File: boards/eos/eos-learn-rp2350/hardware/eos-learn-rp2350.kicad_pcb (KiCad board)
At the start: 4 copper layers, 52.6 x 51.6 mm, 53 parts, among them J1 USB-C, J2 GPIO 0-15, J3 Power, GPIO 16-29, J4 SWD, J5 Qwiic, SW1 BOOTSEL, SW2 RUN, U1 RP2350A, U2 USBLC6-2SC6, U3 AP7361C-33, U4 W25Q128JVS, Y1 12MHz

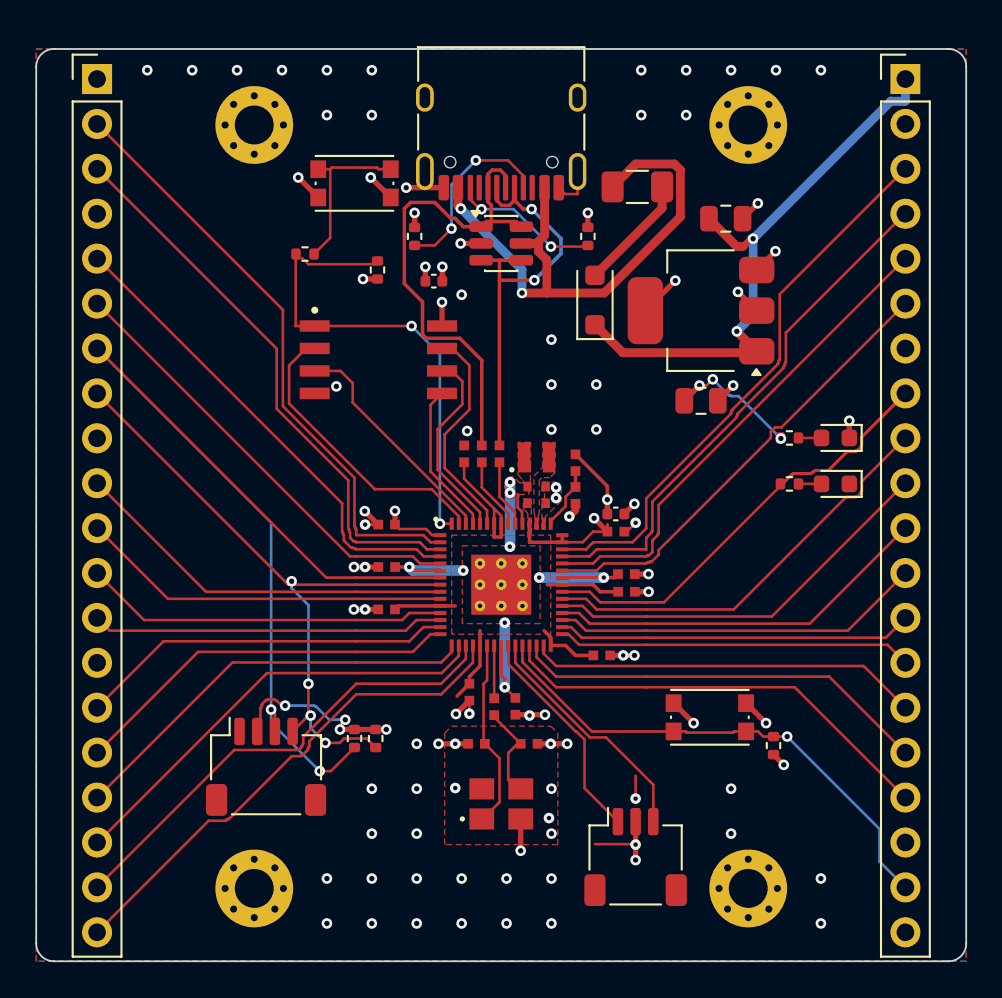
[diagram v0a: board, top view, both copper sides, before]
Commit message: fix(boards): USB-C receptacles at HRO's recommended edge distance
Each HRO TYPE-C-31-M-12 now sits with its footprint origin 3.19 mm from the
board edge it faces (design.USB_C_EDGE). HRO's "RECOMMEND P.C.B LAYOUT" draws
the PCB edge 5.79 mm from the locating pegs, which are 2.60 mm behind the
origin. At the old 3.8 mm the shell's face was 0.15 mm behind the edge, so a
plug's overmold could meet the board before the plug seated; the shell now
stands about 0.46 mm proud of it.

EoS Learn RP2350, EoS Probe S3 and EoS CM5 Base are moved and rebuilt: all
three report ERC 0, DRC errors 0, unconnected 0, schematic parity 0, with the
same DRC warnings as before (4, 4 and 6). On EoS CM5 Base, GPIO2 (the
header's SDA, CM5 pin 58) is now a priority route: after the move the
autorouter boxed its pad in twice, also with 100 passes.

UsbCEdgeTest checks every board's receptacles against the constant, within
the drawing's 0.05 mm tolerance. It fails for the old 3.8 mm placement.

Found in the independent review of a later board (EoS TM4C123 Board, M1).
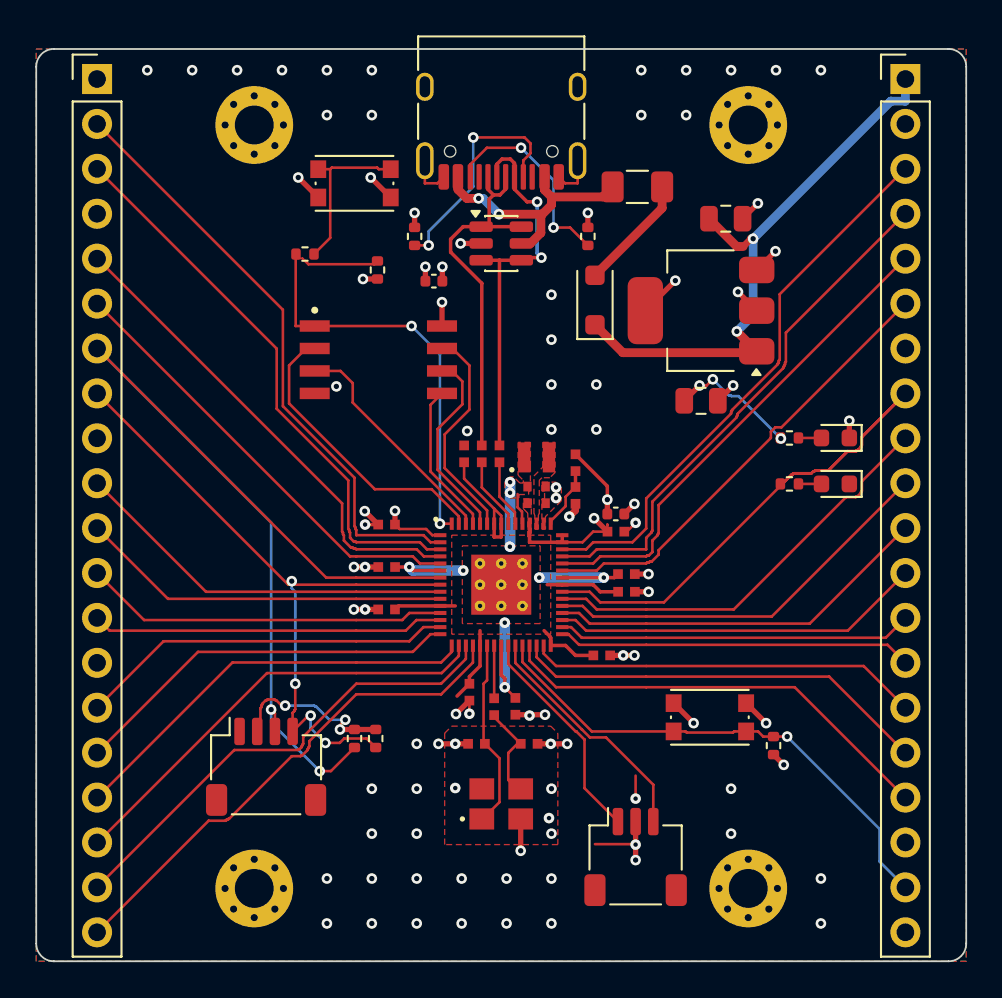
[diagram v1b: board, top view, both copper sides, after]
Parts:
- moved J1 0.61 mm to (26.3, 3.19)
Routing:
- net VBUS: track 32.6 -> 14.7 mm
- net /USB_D+: track 28.6 -> 21.3 mm
- net /CC2: track 8.45 -> 11.6 mm
- net /CC1: track 10.6 -> 13.4 mm
- net /USB_D-: track 23.9 -> 22.2 mm
- net /GPIO5: track 38.6 -> 39.3 mm
- net +3V3: track 61.0 -> 60.4 mm, vias 15 -> 14
- net GND: track 50.9 -> 51.3 mm, vias 89 -> 88

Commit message: fix(boards): rebuild the ten boards made before the no-via-in-pad rule (#55)
PR #64's generator keeps vias out of surface pads (a chip's exposed pad
aside) and 0.1 mm from their own net's pads. Ten boards on master were built
before that rule and had 34 pads with a via in or beside them. They are
rebuilt with the same generator: ATmega328P, RA2E1, KE16Z, KL25, STM32 64,
ESP32 DevKit, Learn RP2350, LPC55S69, CM4 Base and CM5 Base. Each builds at
ERC 0, DRC errors 0, unconnected 0 and parity 0, with the same parts, values,
nets and positions and the same DRC warnings as before.

Where the router could no longer close a short link without a via in a pad,
or left a ground pad without a good path to a via, the design files use
routing options only: priority routes, fanout_first, ground_vias, and a
bottom-layer router keep-out under KL25's crystal (so RESET_b no longer runs
under it). ViaInPadTest drops BUILT_BEFORE_THE_RULE; it now allows only Learn
RP2350's two Raspberry Pi reference vias, named by position. READMEs, TASKS
and CHANGELOG follow the rebuilt copper. Independent verification: three
rounds; the owner adopted a two-layer pour-island criterion (TASKS.md).

Part of #55.
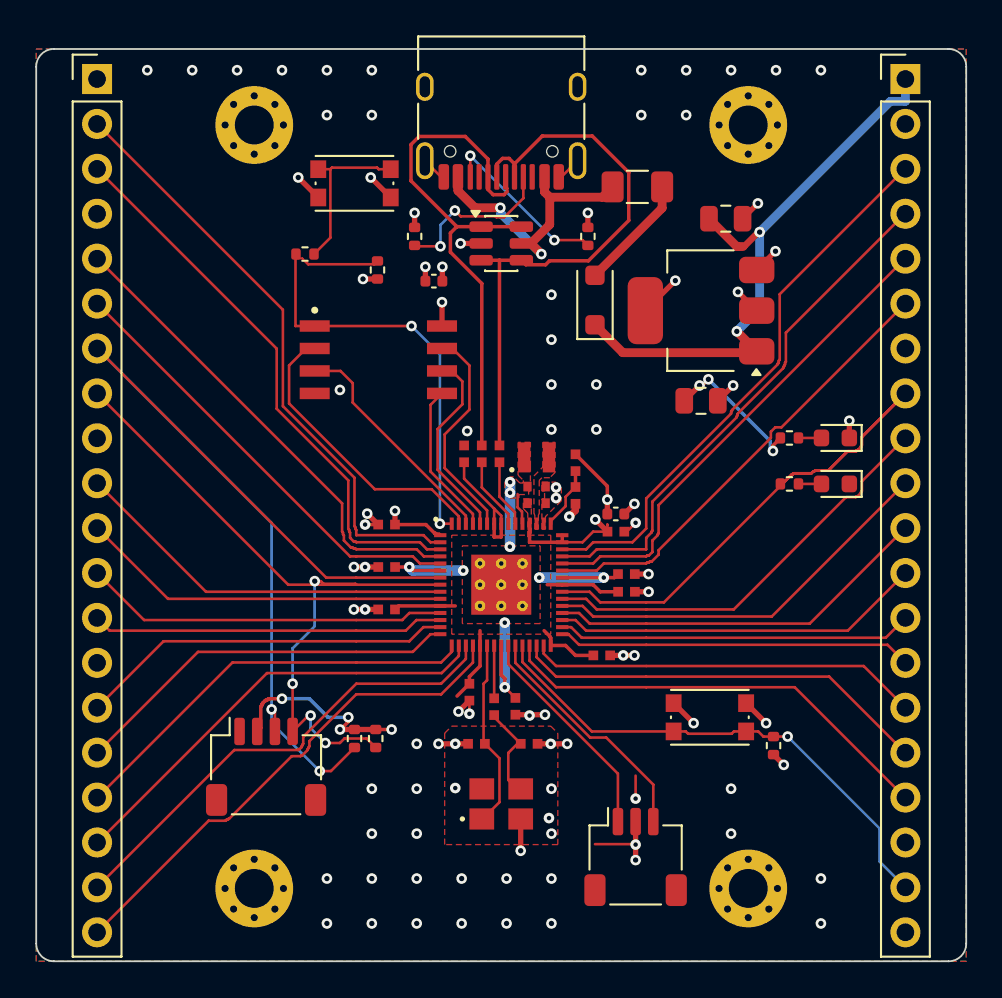
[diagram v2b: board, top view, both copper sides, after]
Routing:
- net /USB_D-: track 22.2 -> 33.4 mm, vias 2 -> 0
- net /USB_D+: track 21.3 -> 31.6 mm
- net /CC1: track 13.4 -> 9.52 mm
- net /GPIO5: track 39.3 -> 41.8 mm
- net GND: track 51.3 -> 48.8 mm
- net VBUS: track 14.7 -> 16.9 mm
- net +3V3: track 60.4 -> 62.5 mm, vias 14 -> 15
- net /CC2: track 11.6 -> 9.96 mm
- net +5V: track 33.5 -> 34.0 mm
